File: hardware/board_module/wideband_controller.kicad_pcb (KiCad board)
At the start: 4 copper layers, 29 x 20.9 mm, 61 parts, among them J1 Conn_01x08, J3 Conn_01x08, J4 FTSH-107-01-F-DV-K, Q1 BTS3028, U1 MCP6004, U2 STM32F042K6Tx, U3 REF3033, U5 AD8628, U9 XC6206P332MR

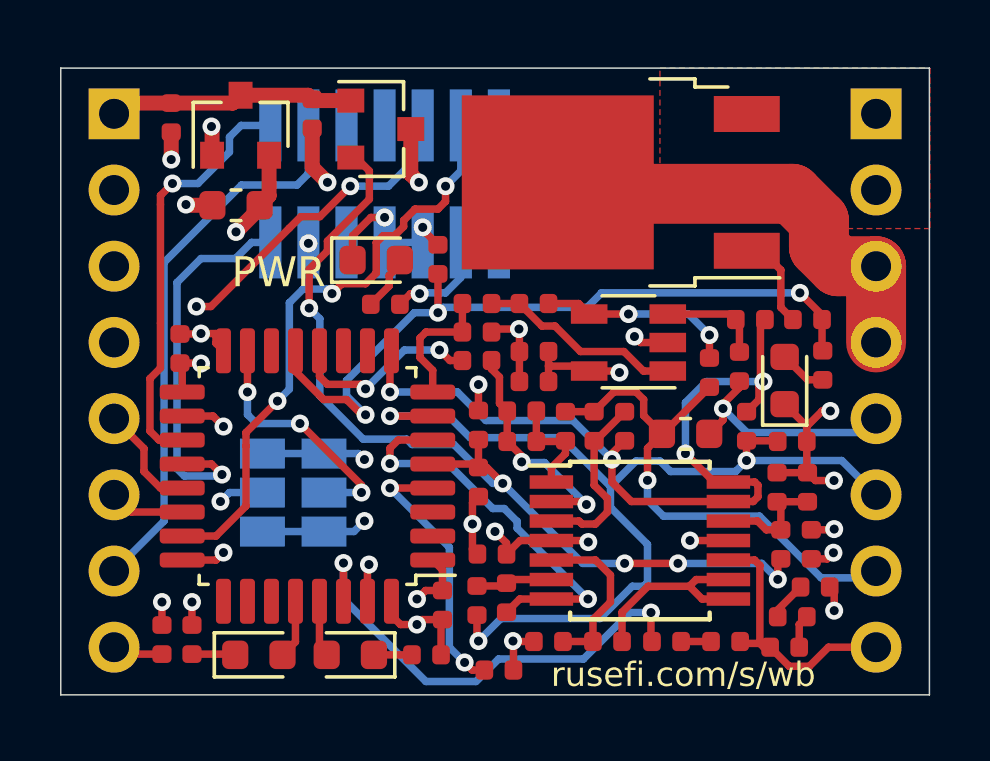
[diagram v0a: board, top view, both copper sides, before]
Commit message: module revision update to kicad 6 break out SEL pins add 4.2/ADV support switch to TC2030 programming header
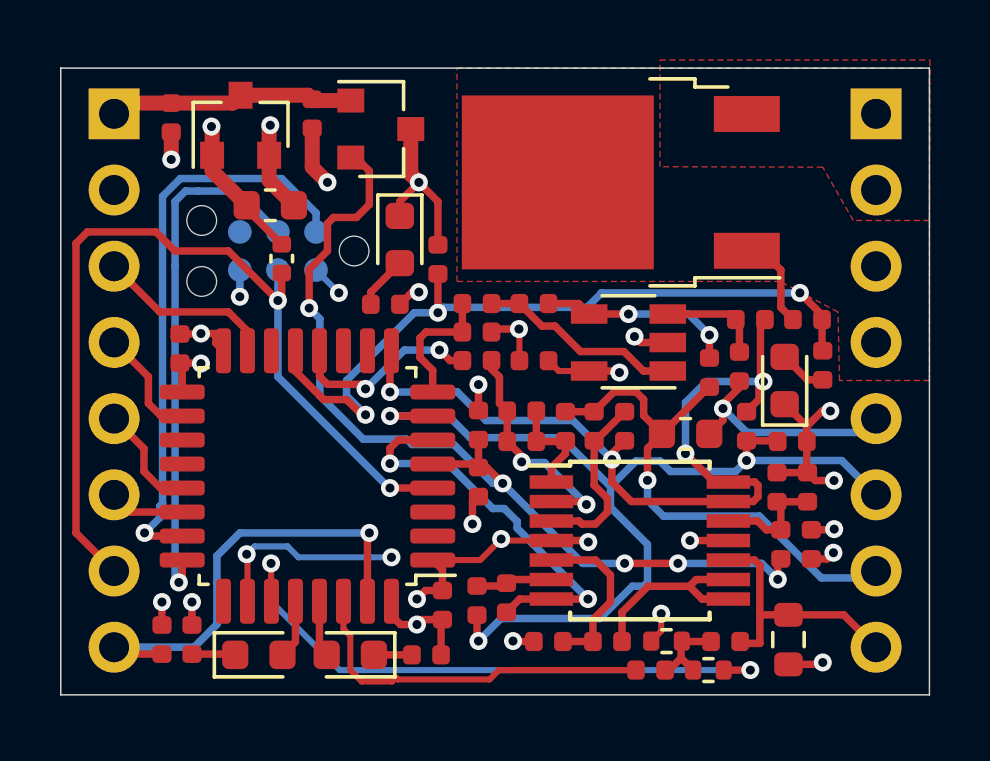
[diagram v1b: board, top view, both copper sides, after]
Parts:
- removed C15, C6: DNP, Capacitor_SMD:C_0402_1005Metric
- removed J4: FTSH-107-01-F-DV-K, Connector_PinHeader_1.27mm:PinHeader_2x07_P1.27mm_Vertical_SMD
- removed JP1, JP2: Jumper_3_Open, Jumper:SolderJumper-3_P1.3mm_Open_Pad1.0x1.5mm
- removed R22: 20k, Resistor_SMD:R_0402_1005Metric
- added J2: Conn_ARM_SWD_TagConnect_TC2030, Connector:Tag-Connect_TC2030-IDC-NL_2x03_P1.27mm_Vertical, B.Cu at (88.3, 79.2)
- added R19: 47k, Resistor_SMD:R_0402_1005Metric, F.Cu at (102.6, 93.2)
- C16: value 1u -> 100n
- R14: value 20k -> 62k; footprint Resistor_SMD:R_0402_1005Metric -> Resistor_SMD:R_0603_1608Metric
- R16: value 20k -> 6.8k
- moved C16 15.5 mm to (88.4, 79.5), turned to 90 degrees
- moved R16 5.27 mm to (101.2, 92.3), turned to 180 degrees
- moved C10 1.14 mm to (88.0, 77.7)
- moved R6 1.09 mm to (100.7, 93.2)
- moved D4 1.04 mm to (92.3, 78.9), turned to -90 degrees
- moved R14 0.77 mm to (105.3, 92.2), turned to 90 degrees
- moved C5 0.69 mm to (96.8, 82.9)
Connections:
- net /Nernst_esr_drive renamed /Nernst_esr_drive_49
- C2 pad 2: Net-(C2-Pad2) -> Net-(R6-Pad1)
- J3 pad 3: (no net) -> /SEL_1
- J3 pad 4: (no net) -> /SEL_2
- R14 pad 1: Net-(R14-Pad1) -> +3V3
- R14 pad 2: Net-(R14-Pad2) -> /LSU_Un
- R16 pad 1: Net-(R14-Pad2) -> Net-(R6-Pad1)
- R16 pad 2: +3V3 -> /Nernst_esr_drive_42
- R6 pad 1: Net-(C2-Pad2) -> Net-(R6-Pad1)
- U2 pad 10: (no net) -> unconnected-(U2-Pad10)
- U2 pad 11: (no net) -> unconnected-(U2-Pad11)
- U2 pad 14: (no net) -> unconnected-(U2-Pad14)
- U2 pad 19: /UART_TX -> unconnected-(U2-Pad19)
- U2 pad 2: (no net) -> unconnected-(U2-Pad2)
- U2 pad 20: /UART_RX -> unconnected-(U2-Pad20)
- U2 pad 25: (no net) -> unconnected-(U2-Pad25)
- U2 pad 26: (no net) -> /Nernst_esr_drive_42
- U2 pad 27: (no net) -> /Nernst_esr_drive_adv
- U2 pad 3: (no net) -> unconnected-(U2-Pad3)
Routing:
- net /Nernst_esr_drive_adv: track 0.00 -> 20.3 mm, vias 0 -> 2
- net /Nernst_esr_drive_42: track 0.00 -> 17.5 mm, vias 0 -> 3
- net Net-(J1-Pad3): track 15.4 -> 0.54 mm
- net /UART_TX: track 14.2 -> 0.00 mm, vias 1 -> 0
- net /UART_RX: track 13.1 -> 0.00 mm, vias 1 -> 0
- net /nRESET: track 38.8 -> 30.5 mm
- net GND: track 39.1 -> 34.8 mm, vias 22 -> 18
- net +3V3: track 22.8 -> 18.7 mm
- net /SWCLK: track 21.6 -> 17.7 mm, vias 3 -> 1
- net /Nernst_esr_drive_49: track 15.8 -> 12.3 mm, vias 2 -> 0
- net Net-(R6-Pad1): track 0.00 -> 2.77 mm
- net /SEL_2: track 6.47 -> 3.81 mm, vias 2 -> 0
- net /SEL_1: track 8.40 -> 6.00 mm, vias 3 -> 0
- net /Boot0: track 13.3 -> 15.4 mm
- net Net-(R14-Pad2): track 1.31 -> 0.00 mm
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- added copper zone on F.Cu, net Net-(J1-Pad3)
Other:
- net class Default removed
- board text removed: "1"
- board text removed: "2"
- board text removed: "PWR"
- board text removed: "rusefi.com/s/wb"

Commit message: vbatt sense
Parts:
- added C6: 1u, Capacitor_SMD:C_0402_1005Metric, F.Cu at (88.8, 79.4)
- added R20: 100k, Resistor_SMD:R_0402_1005Metric, F.Cu at (86.9, 79.4)
- added R21: 10k, Resistor_SMD:R_0402_1005Metric, F.Cu at (87.8, 79.4)
- moved C16 1.93 mm to (89.5, 81.1), turned to 0 degrees
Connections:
- J3 pad 7: /nRESET -> /VBatt_Sense
- U2 pad 14: unconnected-(U2-Pad14) -> Net-(U2-Pad14)
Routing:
- net /nRESET: track 30.5 -> 11.1 mm
- net /VBatt_Sense: track 0.00 -> 17.4 mm
- net Net-(U2-Pad14): track 0.00 -> 4.82 mm
- net GND: track 34.8 -> 38.1 mm
- net VDDA: track 32.0 -> 31.4 mm

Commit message: update kicad & bom tweaks
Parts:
- Q1: value BTS3028 -> VND14NV04

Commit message: rev C: just BOM improvements
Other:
- board text added: "github.com/ mck1117/wideband FOME.Tech Happy Cactus Garage Rev C 3/2026"
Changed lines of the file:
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@@
 		(legacy_teardrops no)
 	)
-	(paper "A4")
+	(paper "A5")
+	(title_block
+		(title "FOME Open Source Wideband O2 Module")
+		(date "2026-03-22")
+		(rev "C")
+		(company "FOME / Happy Cactus Garage")
+		(comment 1 "github.com/mck1117/wideband")
+	)
 	(layers
 		(0 "F.Cu" signal)
@@
 		)
 	)
+	(gr_text "github.com/\n	mck1117/wideband\nFOME.Tech\nHappy Cactus Garage\nRev C 3/2026"
+		(at 98.7 93.175 270)
+		(layer "B.SilkS")
+		(effects
+			(font
+				(size 1 1)
+				(thickness 0.15)
+			)
+			(justify left bottom mirror)
+		)
+	)
